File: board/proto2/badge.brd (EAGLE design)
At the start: 160 x 100 mm, 12 parts

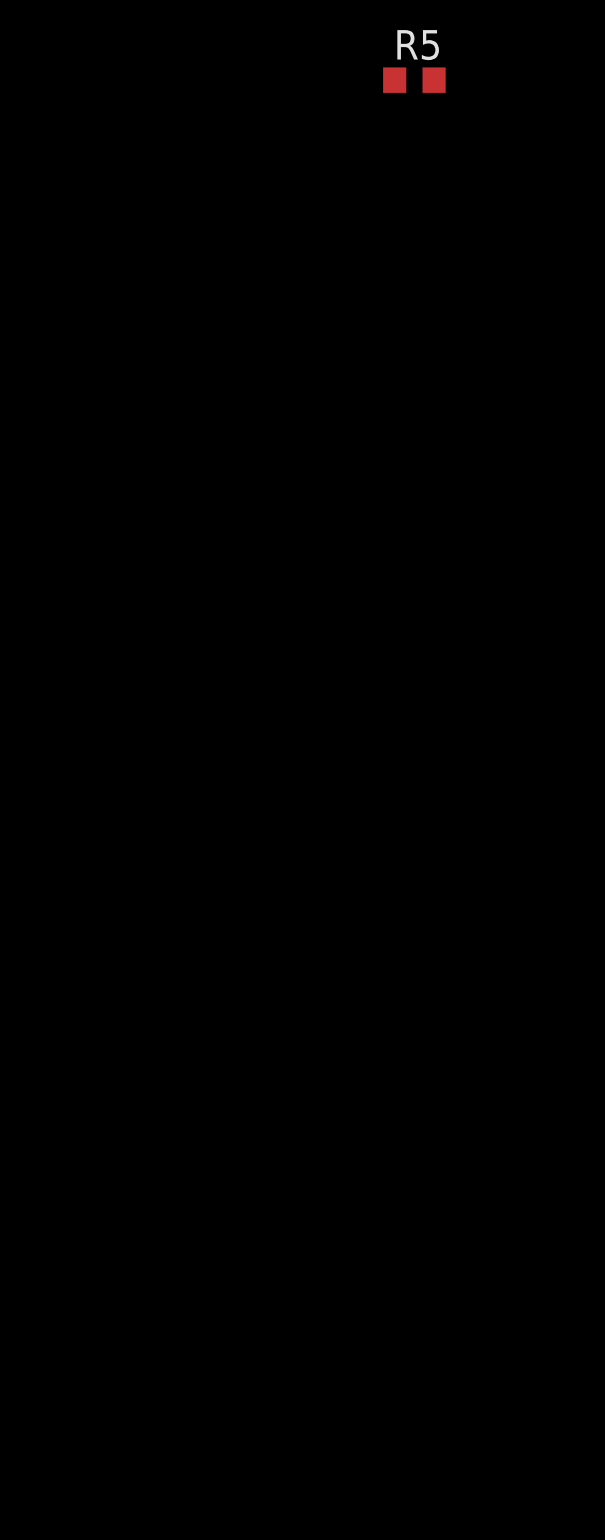
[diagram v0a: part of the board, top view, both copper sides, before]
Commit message: added power suppy to proto2
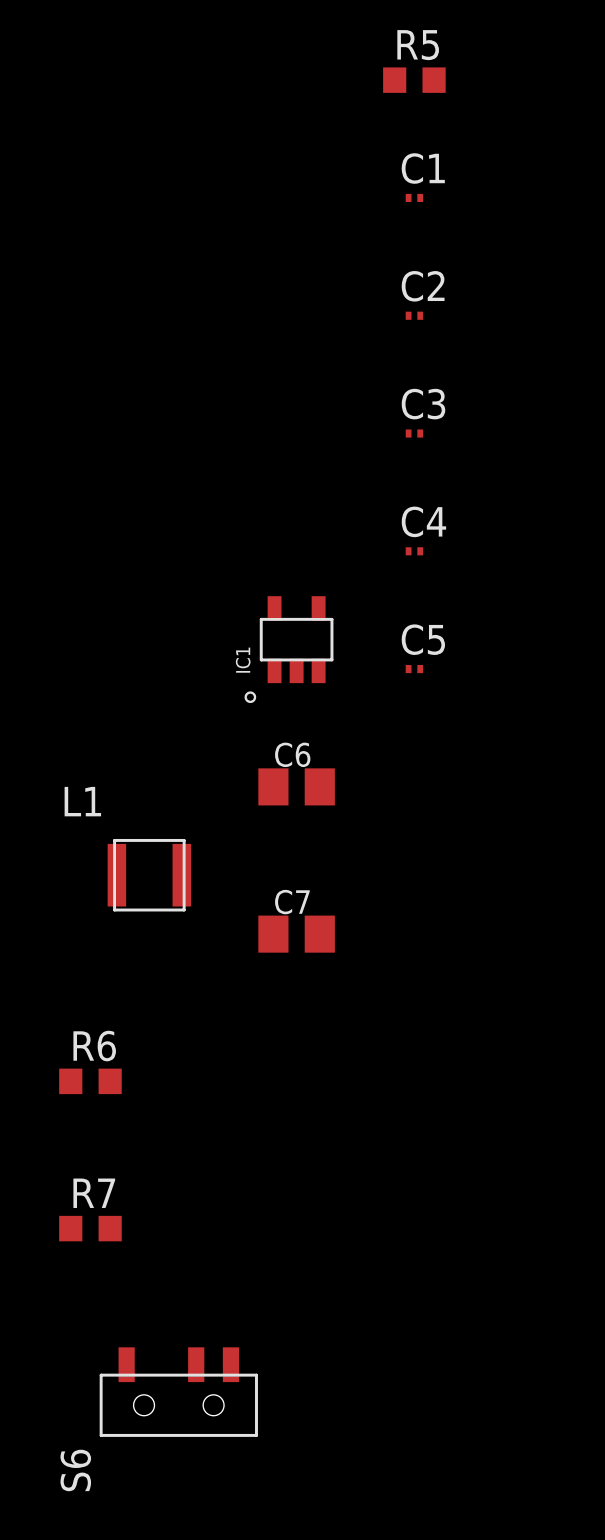
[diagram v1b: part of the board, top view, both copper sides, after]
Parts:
- added C1, C2, C3, C4, C5: .1u, rcl:C0201
- added C6, C7: 10u, rcl:C0805K
- added IC1: TLV62569, badge:DBV-5
- added L1: NR3015T1R0N, badge:NR3015
- added R6: 453k, rcl:R0603
- added R7: 97.6k, rcl:R0603
- added S6: SSSS810701, badge:SSSS810701
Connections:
- new net +3V3: C7.1, L1.2, R6.2, U1.P17
- new net GND: B1.-, C1.2, C2.2, C3.2, C4.2, C5.2, C6.2, C7.2, IC1.2, R7.1, S1.1, S1.2, S2.1, S2.2, S3.1, S3.2, S4.1, S4.2, S5.1, S5.2, U1.P1, U1.P16, U1.P18, U1.P2, U1.P29, U1.P3, U1.P30, U1.P4, U1.P45, U1.P46, U1.P47, U1.P5
- new net N$10: B1.+, S6.3
- new net N$11: C6.1, IC1.1, IC1.4, S6.2
- new net N$12: IC1.5, R6.1, R7.2
- new net N$14: IC1.3, L1.1
- net N$1: now also C1.1
- net N$2: now also C2.1
- net N$3: now also C3.1
- net N$4: now also C4.1
- net N$5: now also C5.1
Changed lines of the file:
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@@
 <element name="R4" library="rcl" package="R0603" value="1.0k" x="-45.72" y="-142.24"/>
 <element name="R5" library="rcl" package="R0603" value="1.0k" x="-45.72" y="-148.59"/>
+<element name="C1" library="rcl" package="C0201" value=".1u" x="-45.72" y="-153.67"/>
+<element name="C2" library="rcl" package="C0201" value=".1u" x="-45.72" y="-158.75"/>
+<element name="C3" library="rcl" package="C0201" value=".1u" x="-45.72" y="-163.83"/>
+<element name="C4" library="rcl" package="C0201" value=".1u" x="-45.72" y="-168.91"/>
+<element name="C5" library="rcl" package="C0201" value=".1u" x="-45.72" y="-173.99"/>
+<element name="IC1" library="badge" package="DBV-5" value="TLV62569" x="-50.8" y="-172.72"/>
+<element name="C6" library="rcl" package="C0805K" value="10u" x="-50.8" y="-179.07">
+<attribute name="MPN" value="JMK212BJ106KD-T" x="-50.8" y="-179.07" size="1.778" layer="27" display="off"/>
+</element>
+<element name="C7" library="rcl" package="C0805K" value="10u" x="-50.8" y="-185.42">
+<attribute name="MPN" value="JMK212BJ106KD-T" x="-50.8" y="-185.42" size="1.778" layer="27" display="off"/>
+</element>
+<element name="L1" library="badge" package="NR3015" value="NR3015T1R0N" x="-57.15" y="-182.88"/>
+<element name="R6" library="rcl" package="R0603" value="453k" x="-59.69" y="-191.77"/>
+<element name="R7" library="rcl" package="R0603" value="97.6k" x="-59.69" y="-198.12"/>
+<element name="S6" library="badge" package="SSSS810701" value="SSSS810701" x="-55.88" y="-205.74"/>
 </elements>
 <signals>
@@
 <contactref element="S1" pad="3"/>
 <contactref element="R1" pad="1"/>
+<contactref element="C1" pad="1"/>
+<wire x1="-46.57" y1="-123.19" x2="-45.97" y2="-153.67" width="0" layer="19" extent="1-1"/>
 <wire x1="-45.255" y1="-81.085" x2="-46.57" y2="-123.19" width="0" layer="19" extent="1-1"/>
 <wire x1="-41.105" y1="-81.085" x2="-45.255" y2="-81.085" width="0" layer="19" extent="1-1"/>
@@
 <contactref element="S2" pad="3"/>
 <contactref element="R2" pad="1"/>
+<contactref element="C2" pad="1"/>
+<wire x1="-46.57" y1="-129.54" x2="-45.97" y2="-158.75" width="0" layer="19" extent="1-1"/>
 <wire x1="-45.255" y1="-89.975" x2="-46.57" y2="-129.54" width="0" layer="19" extent="1-1"/>
 <wire x1="-41.105" y1="-89.975" x2="-45.255" y2="-89.975" width="0" layer="19" extent="1-1"/>
@@
 <contactref element="S3" pad="3"/>
 <contactref element="R3" pad="1"/>
+<contactref element="C3" pad="1"/>
+<wire x1="-46.57" y1="-135.89" x2="-45.97" y2="-163.83" width="0" layer="19" extent="1-1"/>
 <wire x1="-45.255" y1="-98.865" x2="-46.57" y2="-135.89" width="0" layer="19" extent="1-1"/>
 <wire x1="-41.105" y1="-98.865" x2="-45.255" y2="-98.865" width="0" layer="19" extent="1-1"/>
@@
 <contactref element="S4" pad="3"/>
 <contactref element="R4" pad="1"/>
+<contactref element="C4" pad="1"/>
+<wire x1="-46.57" y1="-142.24" x2="-45.97" y2="-168.91" width="0" layer="19" extent="1-1"/>
 <wire x1="-45.255" y1="-107.755" x2="-46.57" y2="-142.24" width="0" layer="19" extent="1-1"/>
 <wire x1="-41.105" y1="-107.755" x2="-45.255" y2="-107.755" width="0" layer="19" extent="1-1"/>
@@
 <contactref element="S5" pad="3"/>
 <contactref element="R5" pad="1"/>
+<contactref element="C5" pad="1"/>
+<wire x1="-46.57" y1="-148.59" x2="-45.97" y2="-173.99" width="0" layer="19" extent="1-1"/>
 <wire x1="-45.255" y1="-116.645" x2="-46.57" y2="-148.59" width="0" layer="19" extent="1-1"/>
 <wire x1="-41.105" y1="-116.645" x2="-45.255" y2="-116.645" width="0" layer="19" extent="1-1"/>
@@
 <wire x1="-25.89" y1="6.77" x2="-44.87" y2="-148.59" width="0" layer="19" extent="1-1"/>
 </signal>
+<signal name="GND">
+<contactref element="C5" pad="2"/>
+<contactref element="C4" pad="2"/>
+<contactref element="C3" pad="2"/>
+<contactref element="C2" pad="2"/>
+<contactref element="C1" pad="2"/>
+<contactref element="U1" pad="P16"/>
+<contactref element="U1" pad="P1"/>
+<contactref element="U1" pad="P2"/>
+<contactref element="U1" pad="P3"/>
+<contactref element="U1" pad="P4"/>
+<contactref element="U1" pad="P5"/>
+<contactref element="U1" pad="P47"/>
+<contactref element="U1" pad="P18"/>
+<contactref element="U1" pad="P29"/>
+<contactref element="U1" pad="P30"/>
+<contactref element="U1" pad="P46"/>
+<contactref element="U1" pad="P45"/>
+<contactref element="S1" pad="1"/>
+<contactref element="S1" pad="2"/>
+<contactref element="S5" pad="1"/>
+<contactref element="S5" pad="2"/>
+<contactref element="S4" pad="1"/>
+<contactref element="S4" pad="2"/>
+<contactref element="S3" pad="1"/>
+<contactref element="S3" pad="2"/>
+<contactref element="S2" pad="1"/>
+<contactref element="S2" pad="2"/>
+<contactref element="IC1" pad="2"/>
+<contactref element="B1" pad="-"/>
+<contactref element="C6" pad="2"/>
+<contactref element="C7" pad="2"/>
+<contactref element="R7" pad="1"/>
+<wire x1="-49.8" y1="-179.07" x2="-49.8" y2="-185.42" width="0" layer="19" extent="1-1"/>
+<wire x1="-50.8" y1="-174.07" x2="-49.8" y2="-179.07" width="0" layer="19" extent="1-1"/>
+<wire x1="-45.47" y1="-173.99" x2="-50.8" y2="-174.07" width="0" layer="19" extent="1-1"/>
+<wire x1="-45.47" y1="-168.91" x2="-45.47" y2="-173.99" width="0" layer="19" extent="1-1"/>
+<wire x1="-45.47" y1="-163.83" x2="-45.47" y2="-168.91" width="0" layer="19" extent="1-1"/>
+<wire x1="-45.47" y1="-158.75" x2="-45.47" y2="-163.83" width="0" layer="19" extent="1-1"/>
+<wire x1="-45.47" y1="-153.67" x2="-45.47" y2="-158.75" width="0" layer="19" extent="1-1"/>
+<wire x1="-60.54" y1="-198.12" x2="-49.8" y2="-185.42" width="0" layer="19" extent="1-1"/>
+<wire x1="-45.255" y1="-114.495" x2="-45.47" y2="-153.67" width="0" layer="19" extent="1-1"/>
+<wire x1="-41.105" y1="-114.495" x2="-45.255" y2="-114.495" width="0" layer="19" extent="1-1"/>
+<wire x1="-45.255" y1="-105.605" x2="-45.255" y2="-114.495" width="0" layer="19" extent="1-1"/>
+<wire x1="-41.105" y1="-105.605" x2="-45.255" y2="-105.605" width="0" layer="19" extent="1-1"/>
+<wire x1="-45.255" y1="-96.715" x2="-45.255" y2="-105.605" width="0" layer="19" extent="1-1"/>
+<wire x1="-41.105" y1="-96.715" x2="-45.255" y2="-96.715" width="0" layer="19" extent="1-1"/>
+<wire x1="-45.255" y1="-87.825" x2="-45.255" y2="-96.715" width="0" layer="19" extent="1-1"/>
+<wire x1="-41.105" y1="-87.825" x2="-45.255" y2="-87.825" width="0" layer="19" extent="1-1"/>
+<wire x1="-45.255" y1="-78.935" x2="-45.255" y2="-87.825" width="0" layer="19" extent="1-1"/>
+<wire x1="-41.105" y1="-78.935" x2="-45.255" y2="-78.935" width="0" layer="19" extent="1-1"/>
+<wire x1="-22.52" y1="-17.75" x2="-41.105" y2="-78.935" width="0" layer="19" extent="1-1"/>
+<wire x1="-24.99" y1="1.82" x2="-22.52" y2="-17.75" width="0" layer="19" extent="1-1"/>
+<wire x1="-26.09" y1="1.82" x2="-24.99" y2="1.82" width="0" layer="19" extent="1-1"/>
+<wire x1="-32.14" y1="2.72" x2="-26.09" y2="1.82" width="0" layer="19" extent="1-1"/>
+<wire x1="-33.79" y1="1.82" x2="-32.14" y2="2.72" width="0" layer="19" extent="1-1"/>
+<wire x1="-33.79" y1="8.42" x2="-32.14" y2="2.72" width="0" layer="19" extent="1-1"/>
+<wire x1="-32.89" y1="8.97" x2="-33.79" y2="8.42" width="0" layer="19" extent="1-1"/>
+<wire x1="-33.79" y1="9.52" x2="-32.89" y2="8.97" width="0" layer="19" extent="1-1"/>
+<wire x1="-32.89" y1="10.07" x2="-33.79" y2="9.52" width="0" layer="19" extent="1-1"/>
+<wire x1="-33.79" y1="10.62" x2="-32.89" y2="10.07" width="0" layer="19" extent="1-1"/>
+<wire x1="-31.04" y1="10.62" x2="-32.89" y2="10.07" width="0" layer="19" extent="1-1"/>
+<wire x1="-27.74" y1="10.62" x2="-31.04" y2="10.62" width="0" layer="19" extent="1-1"/>
+<wire x1="-24.99" y1="10.62" x2="-27.74" y2="10.62" width="0" layer="19" extent="1-1"/>
+</signal>
+<signal name="N$10">
+<contactref element="B1" pad="+"/>
+<contactref element="S6" pad="3"/>
+<wire x1="-53.63" y1="-203.99" x2="-35.32" y2="-17.75" width="0" layer="19" extent="1-1"/>
+</signal>
+<signal name="N$11">
+<contactref element="IC1" pad="4"/>
+<contactref element="IC1" pad="1"/>
+<contactref element="C6" pad="1"/>
+<contactref element="S6" pad="2"/>
+<wire x1="-51.75" y1="-174.07" x2="-51.8" y2="-179.07" width="0" layer="19" extent="1-1"/>
+<wire x1="-49.85" y1="-171.37" x2="-51.75" y2="-174.07" width="0" layer="19" extent="1-1"/>
+<wire x1="-55.13" y1="-203.99" x2="-51.8" y2="-179.07" width="0" layer="19" extent="1-1"/>
+</signal>
+<signal name="+3V3">
+<contactref element="C7" pad="1"/>
+<contactref element="L1" pad="2"/>
+<contactref element="R6" pad="2"/>
+<contactref element="U1" pad="P17"/>
+<wire x1="-55.75" y1="-182.88" x2="-58.84" y2="-191.77" width="0" layer="19" extent="1-1"/>
+<wire x1="-51.8" y1="-185.42" x2="-55.75" y2="-182.88" width="0" layer="19" extent="1-1"/>
+<wire x1="-32.69" y1="1.82" x2="-55.75" y2="-182.88" width="0" layer="19" extent="1-1"/>
+</signal>
+<signal name="N$14">
+<contactref element="IC1" pad="3"/>
+<contactref element="L1" pad="1"/>
+<wire x1="-49.85" y1="-174.07" x2="-58.55" y2="-182.88" width="0" layer="19" extent="1-1"/>
+</signal>
+<signal name="N$12">
+<contactref element="R6" pad="1"/>
+<contactref element="R7" pad="2"/>
+<contactref element="IC1" pad="5"/>
+<wire x1="-58.84" y1="-198.12" x2="-60.54" y2="-191.77" width="0" layer="19" extent="1-1"/>
+<wire x1="-51.75" y1="-171.37" x2="-60.54" y2="-191.77" width="0" layer="19" extent="1-1"/>
+</signal>
 </signals>

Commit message: adding additional parts
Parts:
- added J1: 5051101092, badge:5051101092
- added R8: 47, rcl:R0603
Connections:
- new net N$13: J1.1, R8.1
- new net P0.08: J1.10, U1.P24
- new net P0.11: J1.9, U1.P27
- new net P0.12: J1.8, U1.P28
- new net P0.13: J1.7, U1.P31
- new net P0.14: J1.6, U1.P32
- new net P0.15: U1.P33
- new net P0.16: U1.P34
- net +3V3: now also J1.3, J1.4, R8.2
- net GND: now also J1.2, J1.5, J1.G1, J1.G2
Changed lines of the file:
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@@
 <element name="R7" library="rcl" package="R0603" value="97.6k" x="-59.69" y="-198.12"/>
 <element name="S6" library="badge" package="SSSS810701" value="SSSS810701" x="-55.88" y="-205.74"/>
+<element name="R8" library="rcl" package="R0603" value="47" x="-59.69" y="-224.79"/>
+<element name="J1" library="badge" package="5051101092" value="5051101092" x="-53.34" y="-229.87"/>
 </elements>
 <signals>
@@
 <contactref element="C7" pad="2"/>
 <contactref element="R7" pad="1"/>
+<contactref element="J1" pad="2"/>
+<contactref element="J1" pad="5"/>
+<contactref element="J1" pad="G2"/>
+<contactref element="J1" pad="G1"/>
 <wire x1="-49.8" y1="-179.07" x2="-49.8" y2="-185.42" width="0" layer="19" extent="1-1"/>
 <wire x1="-50.8" y1="-174.07" x2="-49.8" y2="-179.07" width="0" layer="19" extent="1-1"/>
@@
 <wire x1="-45.47" y1="-153.67" x2="-45.47" y2="-158.75" width="0" layer="19" extent="1-1"/>
 <wire x1="-60.54" y1="-198.12" x2="-49.8" y2="-185.42" width="0" layer="19" extent="1-1"/>
+<wire x1="-53.09" y1="-229.87" x2="-60.54" y2="-198.12" width="0" layer="19" extent="1-1"/>
+<wire x1="-51.59" y1="-229.87" x2="-53.09" y2="-229.87" width="0" layer="19" extent="1-1"/>
+<wire x1="-48.79" y1="-232.57" x2="-51.59" y2="-229.87" width="0" layer="19" extent="1-1"/>
+<wire x1="-57.89" y1="-232.57" x2="-53.09" y2="-229.87" width="0" layer="19" extent="1-1"/>
 <wire x1="-45.255" y1="-114.495" x2="-45.47" y2="-153.67" width="0" layer="19" extent="1-1"/>
 <wire x1="-41.105" y1="-114.495" x2="-45.255" y2="-114.495" width="0" layer="19" extent="1-1"/>
@@
 <contactref element="R6" pad="2"/>
 <contactref element="U1" pad="P17"/>
+<contactref element="R8" pad="2"/>
+<contactref element="J1" pad="3"/>
+<contactref element="J1" pad="4"/>
 <wire x1="-55.75" y1="-182.88" x2="-58.84" y2="-191.77" width="0" layer="19" extent="1-1"/>
 <wire x1="-51.8" y1="-185.42" x2="-55.75" y2="-182.88" width="0" layer="19" extent="1-1"/>
+<wire x1="-58.84" y1="-224.79" x2="-58.84" y2="-191.77" width="0" layer="19" extent="1-1"/>
+<wire x1="-52.59" y1="-229.87" x2="-58.84" y2="-224.79" width="0" layer="19" extent="1-1"/>
+<wire x1="-52.09" y1="-229.87" x2="-52.59" y2="-229.87" width="0" layer="19" extent="1-1"/>
 <wire x1="-32.69" y1="1.82" x2="-55.75" y2="-182.88" width="0" layer="19" extent="1-1"/>
 </signal>
@@
 <wire x1="-51.75" y1="-171.37" x2="-60.54" y2="-191.77" width="0" layer="19" extent="1-1"/>
 </signal>
+<signal name="N$13">
+<contactref element="R8" pad="1"/>
+<contactref element="J1" pad="1"/>
+<wire x1="-51.09" y1="-229.87" x2="-60.54" y2="-224.79" width="0" layer="19" extent="1-1"/>
+</signal>
+<signal name="P0.14">
+<contactref element="U1" pad="P32"/>
+<contactref element="J1" pad="6"/>
+<wire x1="-25.89" y1="3.47" x2="-53.59" y2="-229.87" width="0" layer="19" extent="1-1"/>
+</signal>
+<signal name="P0.15">
+<contactref element="U1" pad="P33"/>
+</signal>
+<signal name="P0.16">
+<contactref element="U1" pad="P34"/>
+</signal>
+<signal name="P0.11">
+<contactref element="U1" pad="P27"/>
+<contactref element="J1" pad="9"/>
+<wire x1="-27.19" y1="1.82" x2="-55.09" y2="-229.87" width="0" layer="19" extent="1-1"/>
+</signal>
+<signal name="P0.12">
+<contactref element="U1" pad="P28"/>
+<contactref element="J1" pad="8"/>
+<wire x1="-26.64" y1="2.72" x2="-54.59" y2="-229.87" width="0" layer="19" extent="1-1"/>
+</signal>
+<signal name="P0.13">
+<contactref element="U1" pad="P31"/>
+<contactref element="J1" pad="7"/>
+<wire x1="-24.99" y1="2.92" x2="-54.09" y2="-229.87" width="0" layer="19" extent="1-1"/>
+</signal>
+<signal name="P0.08">
+<contactref element="U1" pad="P24"/>
+<contactref element="J1" pad="10"/>
+<wire x1="-28.84" y1="2.72" x2="-55.59" y2="-229.87" width="0" layer="19" extent="1-1"/>
+</signal>
 </signals>

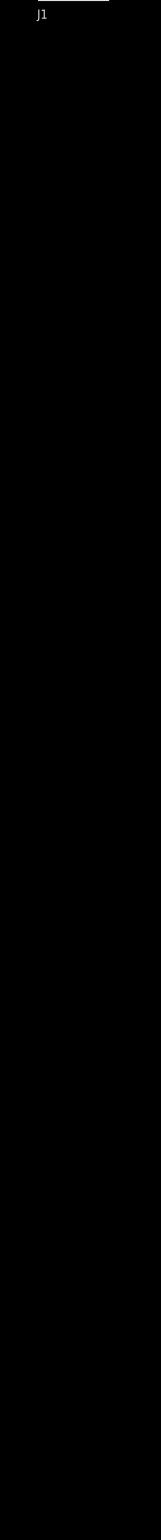
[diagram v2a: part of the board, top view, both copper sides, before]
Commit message: adding bling LEDs to proto2
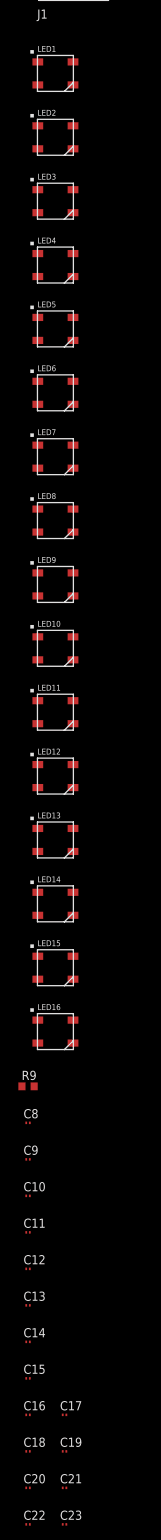
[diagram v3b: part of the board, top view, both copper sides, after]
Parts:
- added C10, C11, C12, C13, C14, C15, C16, C17, C18, C19, C20, C21, C22, C23, C8, C9: .1u, rcl:C0201
- added LED1, LED10, LED11, LED12, LED13, LED14, LED15, LED16, LED2, LED3, LED4, LED5, LED6, LED7, LED8, LED9: WS2812B, badge:WS2812B
- added R9: 47, rcl:R0603
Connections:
- new net N$15: LED5.2, LED6.4
- new net N$16: LED10.4, LED9.2
- new net N$17: LED13.2, LED14.4
- new net N$18: LED1.2, LED2.4
- new net N$19: LED6.2, LED7.4
- new net N$20: LED10.2, LED11.4
- new net N$21: LED14.2, LED15.4
- new net N$22: LED3.2, LED4.4
- new net N$23: LED7.2, LED8.4
- new net N$24: LED2.2, LED3.4
- new net N$25: LED11.2, LED12.4
- new net N$26: LED15.2, LED16.4
- new net N$27: LED4.2, LED5.4
- new net N$28: LED8.2, LED9.4
- new net N$29: LED12.2, LED13.4
- new net N$30: LED1.4, R9.1
- new net P0.02: R9.2, U1.P15
- net +3V3: now also C10.1, C11.1, C12.1, C13.1, C14.1, C15.1, C16.1, C17.1, C18.1, C19.1, C20.1, C21.1, C22.1, C23.1, C8.1, C9.1, LED1.1, LED10.1, LED11.1, LED12.1, LED13.1, LED14.1, LED15.1, LED16.1, LED2.1, LED3.1, LED4.1, LED5.1, LED6.1, LED7.1, LED8.1, LED9.1
- net GND: now also C10.2, C11.2, C12.2, C13.2, C14.2, C15.2, C16.2, C17.2, C18.2, C19.2, C20.2, C21.2, C22.2, C23.2, C8.2, C9.2, LED1.3, LED10.3, LED11.3, LED12.3, LED13.3, LED14.3, LED15.3, LED16.3, LED2.3, LED3.3, LED4.3, LED5.3, LED6.3, LED7.3, LED8.3, LED9.3
